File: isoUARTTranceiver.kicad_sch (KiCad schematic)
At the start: 20 parts, among them U2 TLE9015DQUXUMA1

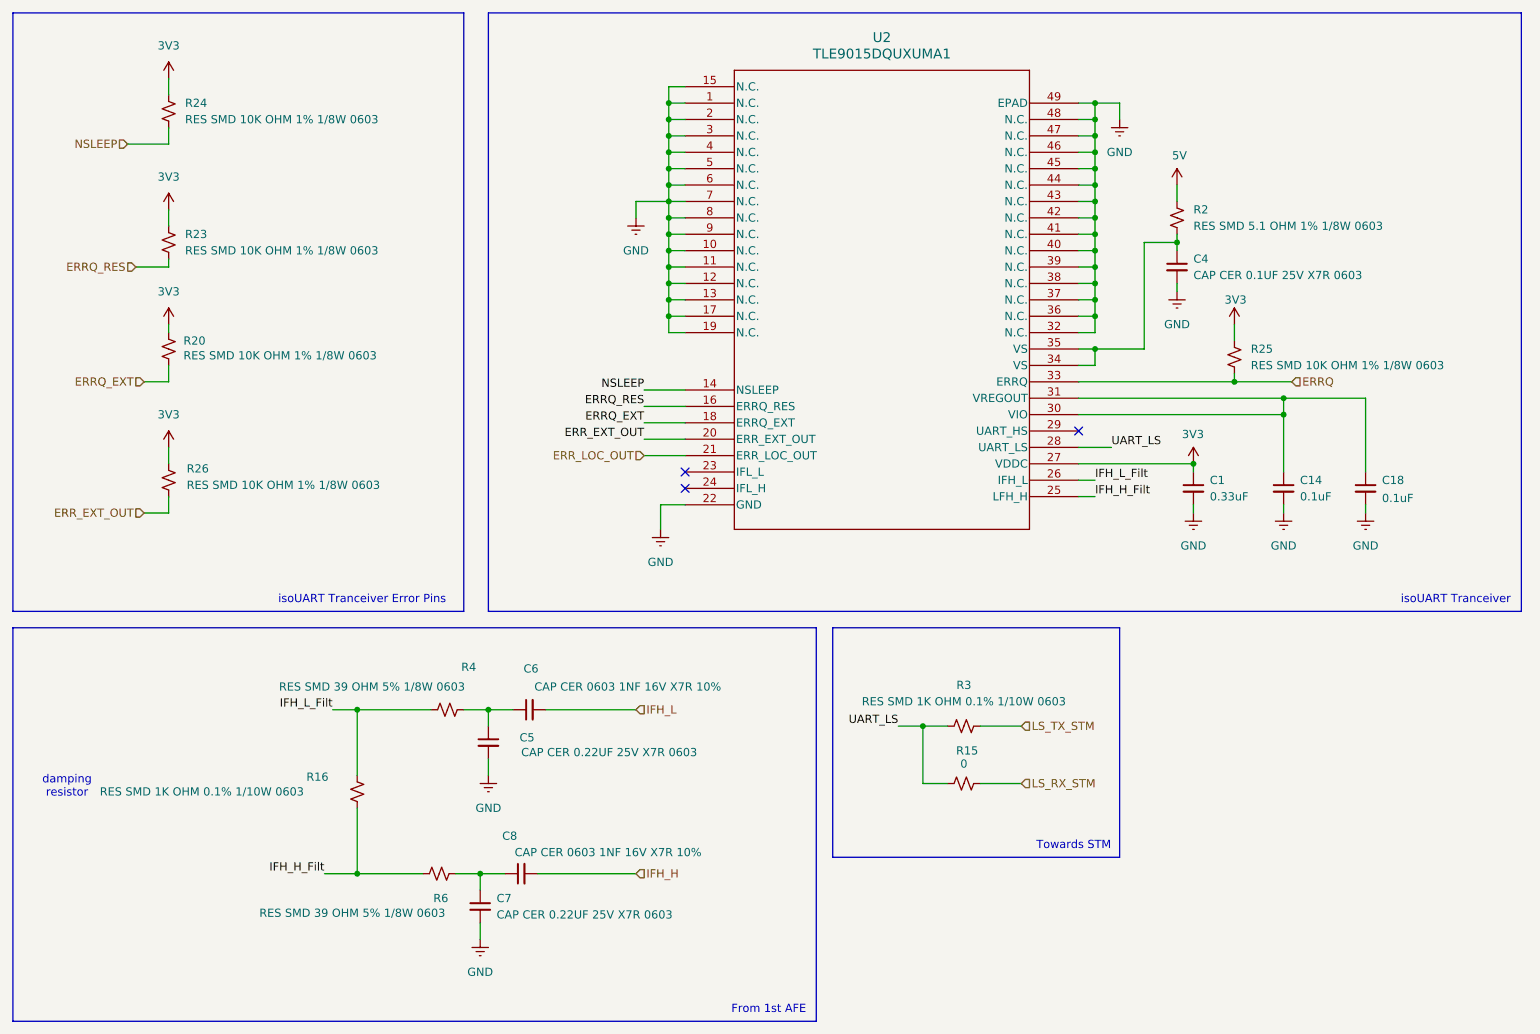
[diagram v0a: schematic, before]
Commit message: initial component placement
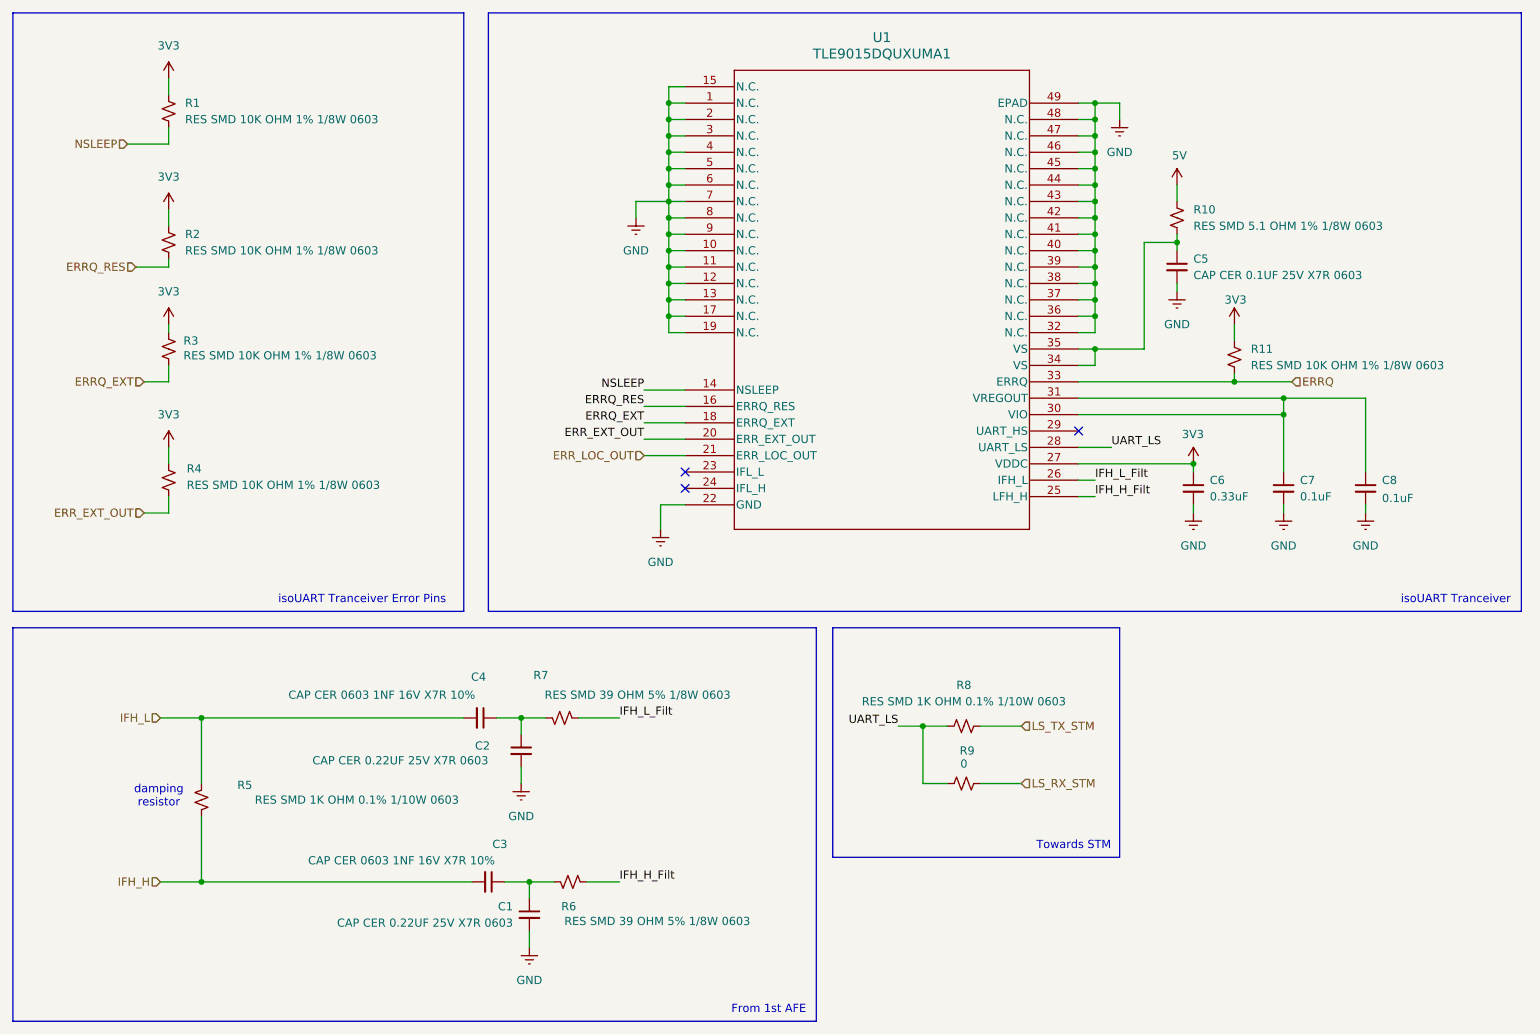
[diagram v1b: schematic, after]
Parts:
- removed R16: RES SMD 1K OHM 0.1% 1/10W 0603, Resistor_SMD:R_0603_1608Metric, symbol Device:R_Small_US
- added R5: RES SMD 1K OHM 0.1% 1/10W 0603, Resistor_SMD:R_0603_1608Metric, symbol Device:R_Small_US
- renumbered C7 to C1, C5 to C2, C8 to C3, C6 to C4, C4 to C5, C1 to C6, C14 to C7, C18 to C8, R24 to R1, R2 to R10, R25 to R11, R23 to R2, R20 to R3, R26 to R4, R4 to R7, R3 to R8, R15 to R9, U2 to U1
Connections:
- net IFH_H: now also R5.1
- net IFH_L: now also R5.2
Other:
- moved on the sheet: C1, C2, C3, C4, R6, R7

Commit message: layout review
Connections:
- net IFH_H renamed IFH_P
- net IFH_H_Filt renamed IFH_Filt_P
- net IFH_L renamed IFH_N
- net IFH_L_Filt renamed IFH_Filt_N
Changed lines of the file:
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@@
 		)
 	)
-	(label "IFH_L_Filt"
+	(label "IFH_Filt_N"
 		(at 199.39 92.71 0)
 		(effects
@@
 		)
 	)
-	(label "IFH_H_Filt"
+	(label "IFH_Filt_P"
 		(at 199.39 95.25 0)
 		(effects
@@
 		)
 	)
-	(label "IFH_H_Filt"
+	(label "IFH_Filt_P"
 		(at 125.73 154.94 0)
 		(effects
@@
 		)
 	)
-	(label "IFH_L_Filt"
+	(label "IFH_Filt_N"
 		(at 125.73 129.54 0)
 		(effects
@@
 		)
 	)
-	(hierarchical_label "IFH_H"
+	(hierarchical_label "IFH_P"
 		(shape input)
 		(at 54.61 154.94 180)
@@
 		)
 	)
-	(hierarchical_label "IFH_L"
+	(hierarchical_label "IFH_N"
 		(shape input)
 		(at 54.61 129.54 180)

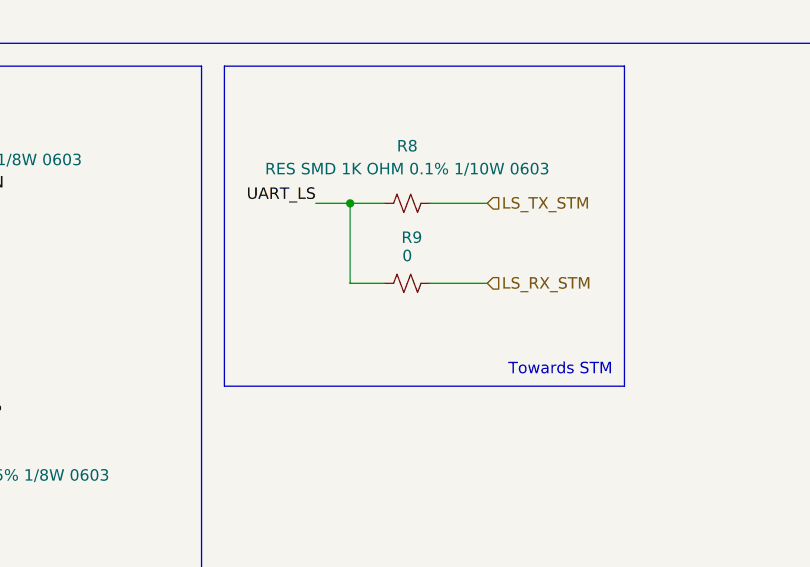
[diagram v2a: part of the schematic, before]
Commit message: layout silkscreens/labels fixed tps added
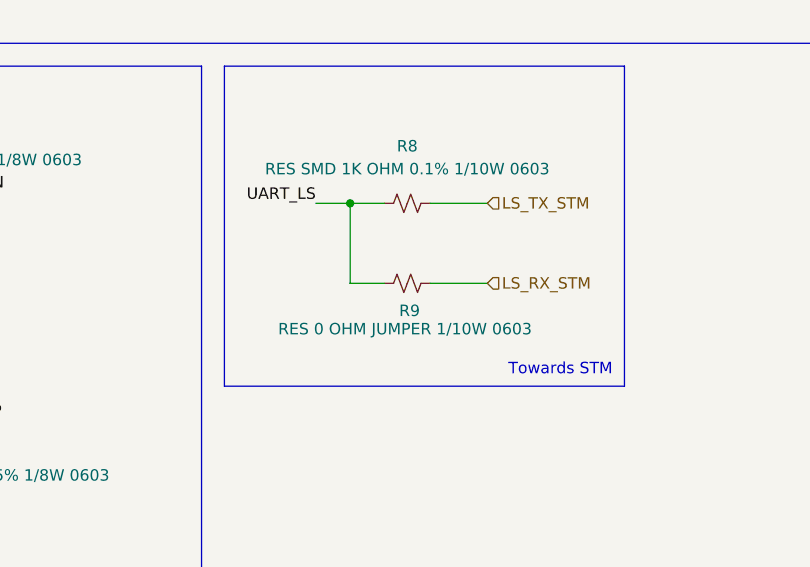
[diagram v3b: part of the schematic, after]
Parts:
- R9: value 0 -> RES 0 OHM JUMPER 1/10W 0603
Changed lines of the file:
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@@
 		(dnp no)
 		(property "Reference" "R9"
-			(at 179.578 134.62 90)
+			(at 179.324 142.748 90)
 			(show_name no)
 			(do_not_autoplace no)
@@
 			)
 		)
-		(property "Value" "0"
-			(at 179.07 136.652 90)
+		(property "Value" "RES 0 OHM JUMPER 1/10W 0603"
+			(at 178.816 144.78 90)
 			(show_name no)
 			(do_not_autoplace no)
@@
 			)
 		)
-		(property "Datasheet" ""
+		(property "Datasheet" "https://www.digikey.ca/en/products/detail/stackpole-electronics-inc/RMCF0603ZT0R00/1756908"
 			(at 179.07 139.7 0)
 			(hide yes)
@@
 			)
 		)
-		(property "Description" "Resistor, small US symbol"
+		(property "Description" "RES 0 OHM JUMPER 1/10W 0603"
 			(at 179.07 139.7 0)
 			(hide yes)
